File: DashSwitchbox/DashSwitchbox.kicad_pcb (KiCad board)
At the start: 2 copper layers, 43.8 x 61 mm, 18 parts, among them J1 Main Connector, J2 Estop Connector, J3 Dash LVMS, J4 To Drive Mode Button, J5 To Drive Mode Switch, J6 AMS Fault LED, J7 BSPD Fault LED, J8 IMD Fault LED, J9 Inertia Fault LED, U1 LD1117V33

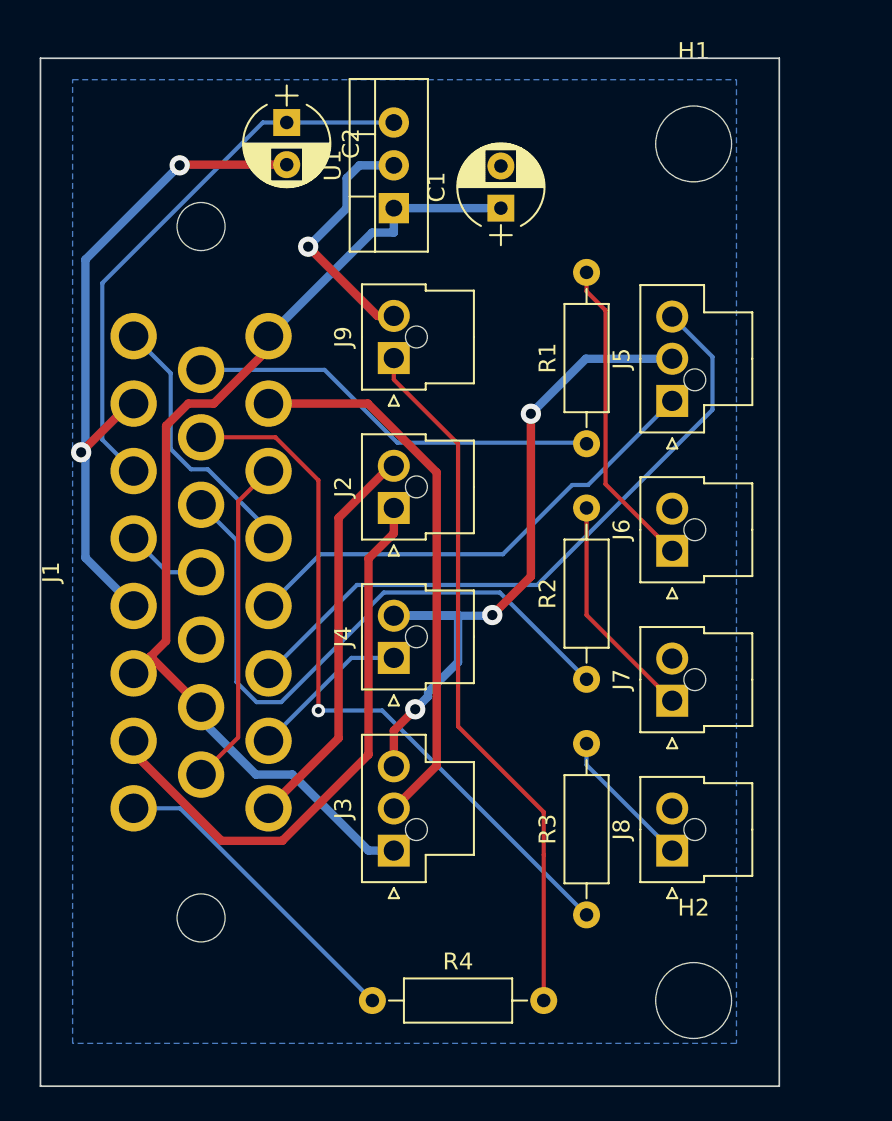
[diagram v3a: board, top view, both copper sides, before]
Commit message: Tweak silkscreen labels on boards for final run
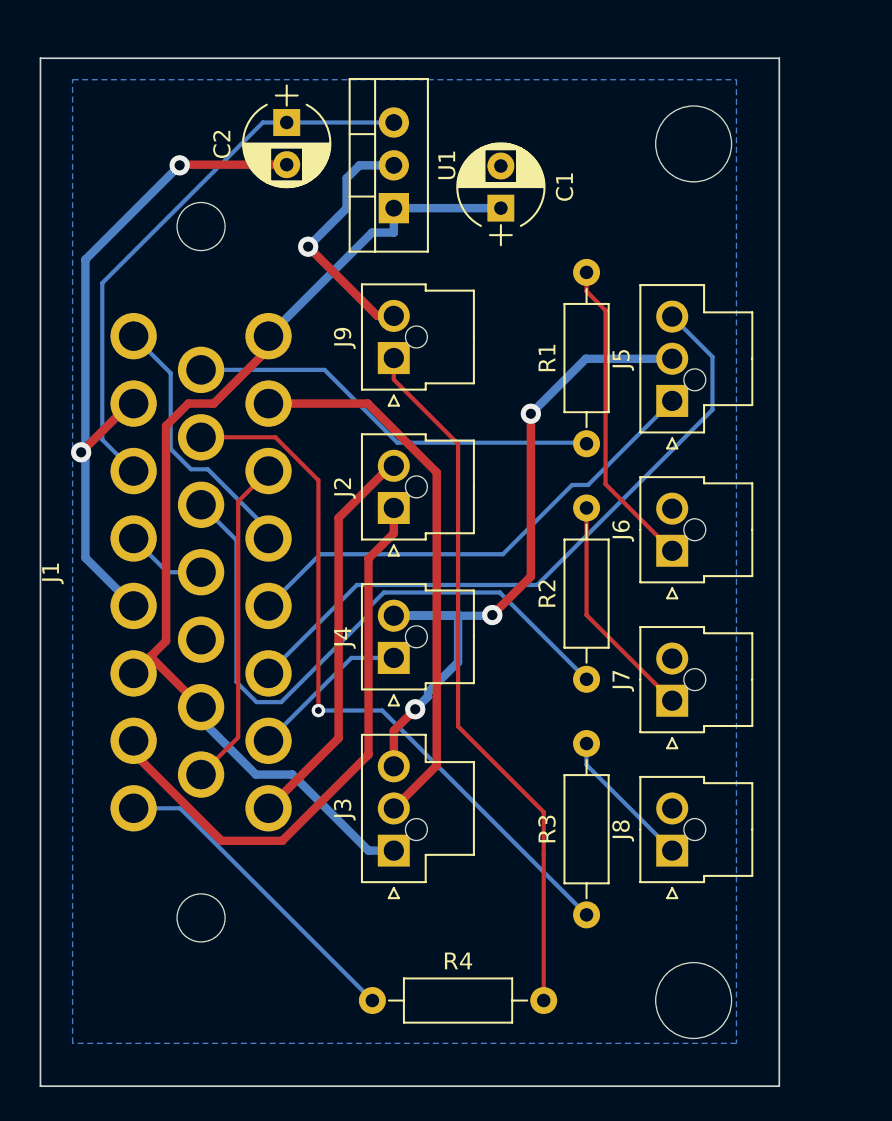
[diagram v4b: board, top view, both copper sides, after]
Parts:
- turned H1 to 180 degrees
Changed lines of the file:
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@@
     (descr "TO-220-3, Vertical, RM 2.54mm")
     (tags "TO-220-3 Vertical RM 2.54mm")
-    (fp_text reference U1 (at 2.54 -3.62 90) (layer F.SilkS)
+    (fp_text reference U1 (at 2.54 3.175 90) (layer F.SilkS)
       (effects (font (size 1 1) (thickness 0.15)))
     )
@@
     (descr "CP, Radial series, Radial, pin pitch=2.50mm, , diameter=5mm, Electrolytic Capacitor")
     (tags "CP Radial series Radial pin pitch 2.50mm  diameter 5mm Electrolytic Capacitor")
-    (fp_text reference C1 (at 1.25 -3.81 90) (layer F.SilkS)
+    (fp_text reference C1 (at 1.27 3.81 90) (layer F.SilkS)
       (effects (font (size 1 1) (thickness 0.15)))
     )
@@
     (descr "CP, Radial series, Radial, pin pitch=2.50mm, , diameter=5mm, Electrolytic Capacitor")
     (tags "CP Radial series Radial pin pitch 2.50mm  diameter 5mm Electrolytic Capacitor")
-    (fp_text reference C2 (at 1.25 -3.81 270) (layer F.SilkS)
+    (fp_text reference C2 (at 1.27 3.81 270) (layer F.SilkS)
       (effects (font (size 1 1) (thickness 0.15)))
     )
@@
   )
   (module Mounting_Holes:MountingHole_4.5mm (layer F.Cu)
-    (at 121.92 73.66)
+    (at 121.92 73.66 180)
     (descr "Mounting Hole 4.5mm, no annular")
     (tags "mounting hole 4.5mm no annular")
     (attr virtual)
-    (fp_text reference H1 (at 0 -5.5) (layer F.SilkS)
-      (effects (font (size 1 1) (thickness 0.15)))
-    )
-    (fp_text value MtngHole (at 0 5.5) (layer F.Fab)
-      (effects (font (size 1 1) (thickness 0.15)))
-    )
-    (fp_text user %R (at 0.3 0) (layer F.Fab)
+    (fp_text reference H1 (at 0 -5.5 180) (layer F.SilkS) hide
+      (effects (font (size 1 1) (thickness 0.15)))
+    )
+    (fp_text value MtngHole (at 0 5.5 180) (layer F.Fab)
+      (effects (font (size 1 1) (thickness 0.15)))
+    )
+    (fp_text user %R (at 0.3 0 180) (layer F.Fab)
       (effects (font (size 1 1) (thickness 0.15)))
     )
     (fp_circle (center 0 0) (end 4.5 0) (layer Cmts.User) (width 0.15))
     (fp_circle (center 0 0) (end 4.75 0) (layer F.CrtYd) (width 0.05))
-    (pad 1 np_thru_hole circle (at 0 0) (size 4.5 4.5) (drill 4.5) (layers *.Cu *.Mask))
+    (pad 1 np_thru_hole circle (at 0 0 180) (size 4.5 4.5) (drill 4.5) (layers *.Cu *.Mask))
   )
   (module Mounting_Holes:MountingHole_4.5mm (layer F.Cu)
@@
     (tags "mounting hole 4.5mm no annular")
     (attr virtual)
-    (fp_text reference H2 (at 0 -5.5) (layer F.SilkS)
-      (effects (font (size 1 1) (thickness 0.15)))
-    )
+    (fp_text reference H2 (at 0 -5.5) (layer F.SilkS) hide
+      (effects (font (size 1 1) (thickness 0.15)))
+    )
